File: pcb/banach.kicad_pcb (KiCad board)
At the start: 2 copper layers, 132.3 x 90.7 mm, 68 parts, among them J1 MJ-4PP-9, J2 OLED, SW10 SW_PUSH, SW11 SW_PUSH, SW12 SW_PUSH, SW14 SW_PUSH, SW15 SW_PUSH, SW16 SW_PUSH, SW17 SW_PUSH, SW18 SW_PUSH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

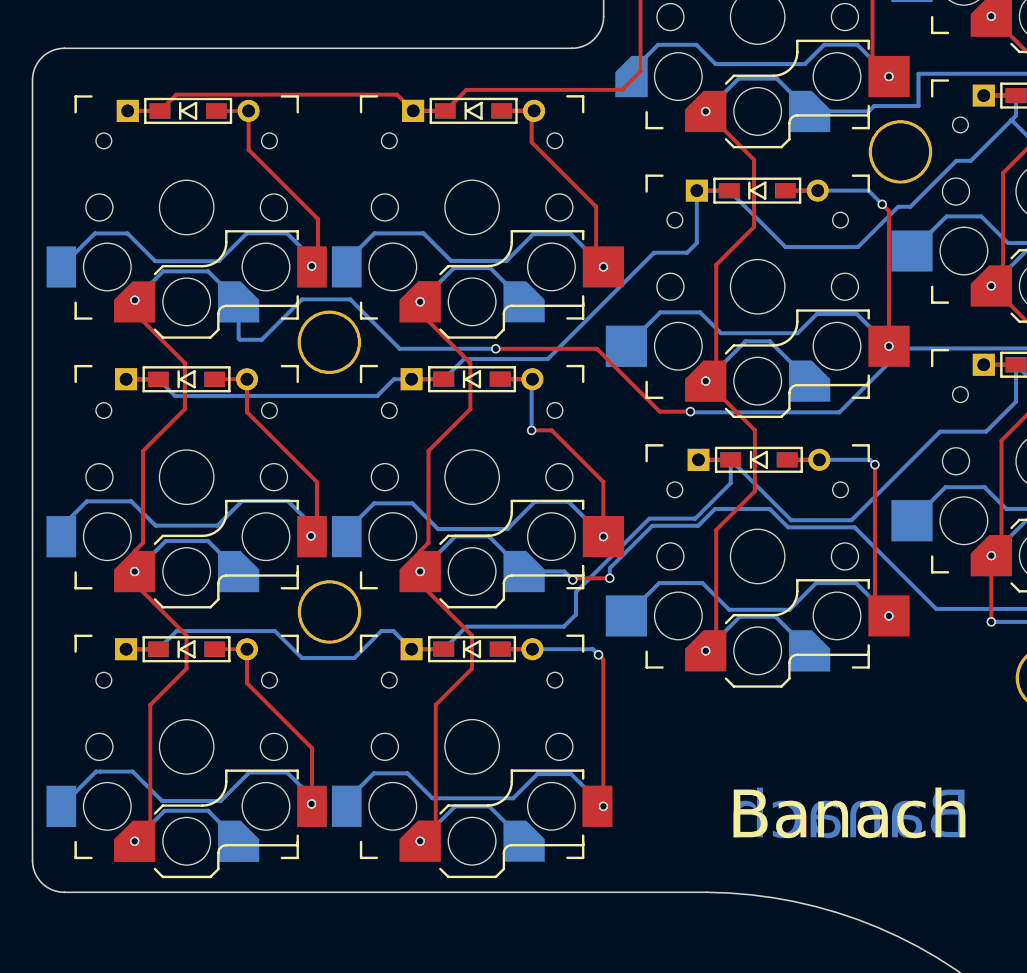
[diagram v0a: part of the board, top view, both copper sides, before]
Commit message: aligned column 0 to true choc spacing
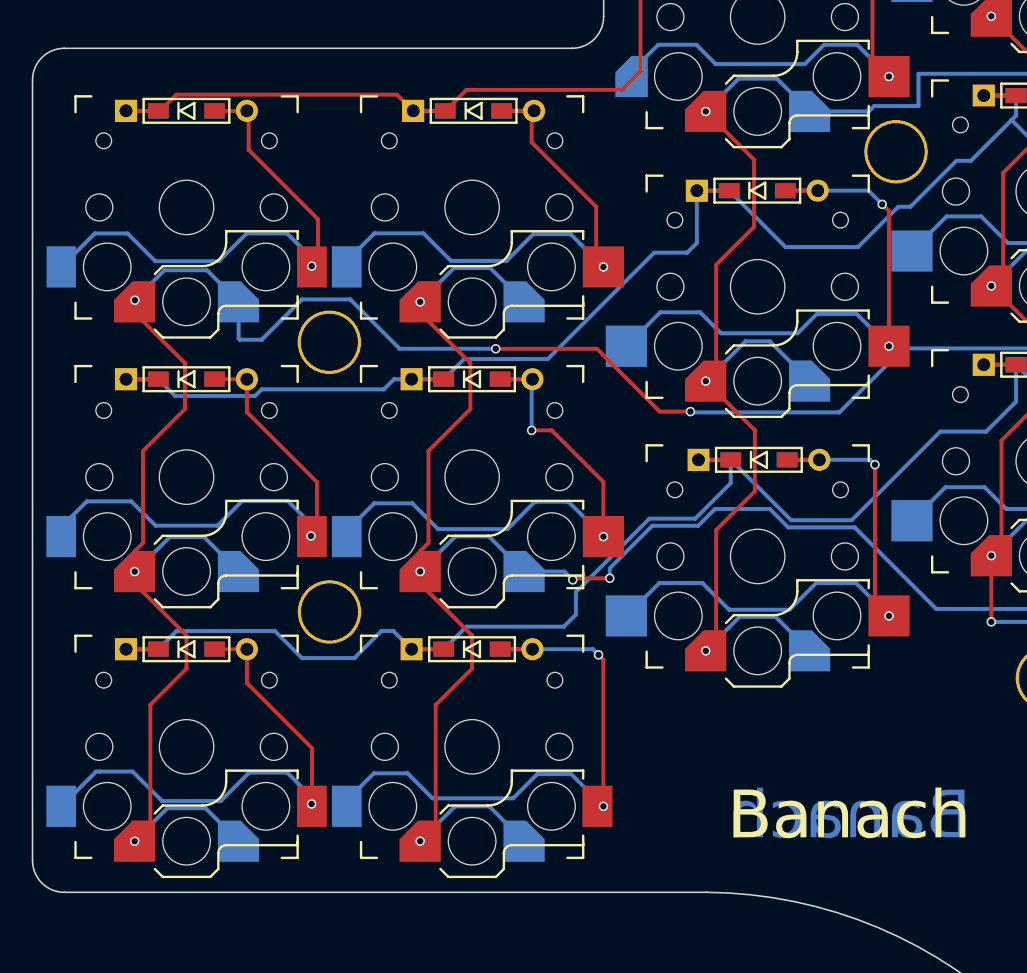
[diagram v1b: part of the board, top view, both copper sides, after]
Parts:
- moved h6 0.28 mm to (112.6, 66.9)
- moved D2 0.11 mm to (67.9, 64.3)
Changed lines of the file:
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@@
   )
   (footprint "kbd:D3_TH_SMD" (layer "F.Cu")
-    (at 67.9088 98.2512)
+    (at 67.9028 98.2472)
     (descr "Resitance 3 pas")
     (tags "R")
@@
   )
   (footprint "kbd:D3_TH_SMD" (layer "F.Cu")
-    (at 68.0104 64.3168)
+    (at 67.9028 64.3128)
     (descr "Resitance 3 pas")
     (tags "R")
@@
   )
   (footprint "keyswitches:Kailh_socket_PG1350_reversible" (layer "F.Cu")
-    (at 67.916 70.404)
+    (at 67.91 70.4)
     (descr "Kailh \"Choc\" PG1350 keyswitch reversible socket mount")
     (tags "kailh,choc")
@@
   )
   (footprint "kbd:LEGO_HOLE" (layer "F.Cu")
-    (at 112.91 66.9)
+    (at 112.63 66.89)
     (descr "Mounting Hole 2.2mm, no annular, M2")
     (tags "mounting hole 2.2mm no annular m2")
@@
   )
   (footprint "kbd:D3_TH_SMD" (layer "F.Cu")
-    (at 67.9088 81.2332)
+    (at 67.9028 81.2292)
     (descr "Resitance 3 pas")
     (tags "R")
@@
   )
   (footprint "keyswitches:Kailh_socket_PG1350_reversible" (layer "F.Cu")
-    (at 67.916 87.404)
+    (at 67.91 87.4)
     (descr "Kailh \"Choc\" PG1350 keyswitch reversible socket mount")
     (tags "kailh,choc")
@@
   )
   (footprint "keyswitches:Kailh_socket_PG1350_reversible" (layer "F.Cu")
-    (at 67.916 104.404)
+    (at 67.91 104.4)
     (descr "Kailh \"Choc\" PG1350 keyswitch reversible socket mount")
     (tags "kailh,choc")
@@
   (segment (start 80.988198 81.2292) (end 82.0928 81.2292) (width 0.25) (layer "B.Cu") (net 2))
   (segment (start 171.27 73.4994) (end 179.45 73.4994) (width 0.25) (layer "B.Cu") (net 2))
+  (segment (start 80.347398 81.87) (end 80.988198 81.2292) (width 0.25) (layer "B.Cu") (net 2))
   (segment (start 102.111 69.342) (end 100.076 69.342) (width 0.25) (layer "B.Cu") (net 2))
   (segment (start 121.7168 66.7004) (end 119.9134 64.897) (width 0.25) (layer "B.Cu") (net 2))
   (segment (start 105.667 72.898) (end 102.111 69.342) (width 0.25) (layer "B.Cu") (net 2))
   (segment (start 165.908303 75.120301) (end 167.529204 73.4994) (width 0.25) (layer "B.Cu") (net 2))
+  (segment (start 67.184299 82.283699) (end 72.226301 82.283699) (width 0.25) (layer "B.Cu") (net 2))
   (segment (start 154.4828 72.4916) (end 152.5524 72.4916) (width 0.25) (layer "B.Cu") (net 2))
+  (segment (start 72.226301 82.283699) (end 72.64 81.87) (width 0.25) (layer "B.Cu") (net 2))
   (segment (start 112.776 70.358) (end 110.236 72.898) (width 0.25) (layer "B.Cu") (net 2))
   (segment (start 133.59632 67.35312) (end 125.16352 67.35312) (width 0.25) (layer "B.Cu") (net 2))
   (segment (start 99.4664 73.2536) (end 97.3836 73.2536) (width 0.25) (layer "B.Cu") (net 2))
-  (segment (start 79.933699 82.283699) (end 80.988198 81.2292) (width 0.25) (layer "B.Cu") (net 2))
   (segment (start 136.144 69.9008) (end 133.59632 67.35312) (width 0.25) (layer "B.Cu") (net 2))
   (segment (start 151.07152 73.97248) (end 142.25068 73.97248) (width 0.25) (layer "B.Cu") (net 2))
@@
   (segment (start 90.6822 79.955) (end 85.402 79.955) (width 0.25) (layer "B.Cu") (net 2))
   (segment (start 110.236 72.898) (end 105.667 72.898) (width 0.25) (layer "B.Cu") (net 2))
-  (segment (start 67.184299 82.283699) (end 79.933699 82.283699) (width 0.25) (layer "B.Cu") (net 2))
+  (segment (start 72.64 81.87) (end 80.347398 81.87) (width 0.25) (layer "B.Cu") (net 2))
   (segment (start 97.3836 73.2536) (end 90.6822 79.955) (width 0.25) (layer "B.Cu") (net 2))
   (segment (start 125.16352 67.35312) (end 124.5108 66.7004) (width 0.25) (layer "B.Cu") (net 2))
@@
   (via (at 64.65 76.25) (size 0.6) (drill 0.4) (layers "F.Cu" "B.Cu") (net 25))
   (segment (start 172.5964 64.6094) (end 179.105002 64.6094) (width 0.25) (layer "B.Cu") (net 25))
-  (segment (start 69.265999 108.428999) (end 66.531001 108.428999) (width 0.25) (layer "B.Cu") (net 25))
+  (segment (start 75.184 76.2) (end 72.644 78.74) (width 0.25) (layer "B.Cu") (net 25))
   (segment (start 99.72 83.32) (end 99.67 83.27) (width 0.25) (layer "B.Cu") (net 25))
+  (segment (start 72.644 78.74) (end 71.262 78.74) (width 0.25) (layer "B.Cu") (net 25))
   (segment (start 152.63 69.92) (end 161.84 69.92) (width 0.25) (layer "B.Cu") (net 25))
+  (segment (start 69.017 91.18) (end 66.85 91.18) (width 0.25) (layer "B.Cu") (net 25))
+  (segment (start 66.69 108.27) (end 64.67 110.29) (width 0.25) (layer "B.Cu") (net 25))
   (segment (start 168.36 66.6794) (end 168.36 64.63) (width 0.25) (layer "B.Cu") (net 25))
-  (segment (start 71.191 93.354) (end 69.265999 91.428999) (width 0.25) (layer "B.Cu") (net 25))
-  (segment (start 64.65 76.22) (end 64.65 76.25) (width 0.25) (layer "B.Cu") (net 25))
   (segment (start 165.0606 66.6994) (end 168.34 66.6994) (width 0.25) (layer "B.Cu") (net 25))
-  (segment (start 71.191 78.669) (end 71.262 78.74) (width 0.25) (layer "B.Cu") (net 25))
-  (segment (start 66.441001 74.428999) (end 64.65 76.22) (width 0.25) (layer "B.Cu") (net 25))
+  (segment (start 71.191 110.354) (end 69.107 108.27) (width 0.25) (layer "B.Cu") (net 25))
+  (segment (start 69.107 108.27) (end 66.69 108.27) (width 0.25) (layer "B.Cu") (net 25))
   (segment (start 78.232 76.2) (end 75.184 76.2) (width 0.25) (layer "B.Cu") (net 25))
+  (segment (start 87.4 79.31) (end 81.342 79.31) (width 0.25) (layer "B.Cu") (net 25))
   (segment (start 168.36 64.63) (end 168.3806 64.6094) (width 0.25) (layer "B.Cu") (net 25))
   (segment (start 181.482 66.986398) (end 181.482 67.1054) (width 0.25) (layer "B.Cu") (net 25))
-  (segment (start 69.265999 74.428999) (end 66.441001 74.428999) (width 0.25) (layer "B.Cu") (net 25))
   (segment (start 142.56 84.6) (end 133.187032 84.6) (width 0.25) (layer "B.Cu") (net 25))
-  (segment (start 75.184 76.2) (end 72.644 78.74) (width 0.25) (layer "B.Cu") (net 25))
   (segment (start 168.3806 64.6094) (end 172.5964 64.6094) (width 0.25) (layer "B.Cu") (net 25))
-  (segment (start 87.4 79.31) (end 81.342 79.31) (width 0.25) (layer "B.Cu") (net 25))
-  (segment (start 66.531001 108.428999) (end 64.67 110.29) (width 0.25) (layer "B.Cu") (net 25))
-  (segment (start 71.262 78.74) (end 72.644 78.74) (width 0.25) (layer "B.Cu") (net 25))
-  (segment (start 71.191 110.354) (end 69.265999 108.428999) (width 0.25) (layer "B.Cu") (net 25))
+  (segment (start 66.51 74.36) (end 64.65 76.22) (width 0.25) (layer "B.Cu") (net 25))
+  (segment (start 64.65 76.22) (end 64.65 76.25) (width 0.25) (layer "B.Cu") (net 25))
   (segment (start 113.0887 79.2913) (end 109.06 83.32) (width 0.25) (layer "B.Cu") (net 25))
   (segment (start 109.06 83.32) (end 99.72 83.32) (width 0.25) (layer "B.Cu") (net 25))
+  (segment (start 168.34 66.6994) (end 168.36 66.6794) (width 0.25) (layer "B.Cu") (net 25))
+  (segment (start 71.262 78.74) (end 71.191 78.669) (width 0.25) (layer "B.Cu") (net 25))
   (segment (start 71.191 78.669) (end 71.191 76.354) (width 0.25) (layer "B.Cu") (net 25))
-  (segment (start 66.601001 91.428999) (end 64.74 93.29) (width 0.25) (layer "B.Cu") (net 25))
-  (segment (start 168.34 66.6994) (end 168.36 66.6794) (width 0.25) (layer "B.Cu") (net 25))
   (segment (start 81.342 79.31) (end 78.232 76.2) (width 0.25) (layer "B.Cu") (net 25))
-  (segment (start 69.265999 91.428999) (end 66.601001 91.428999) (width 0.25) (layer "B.Cu") (net 25))
   (segment (start 133.187032 84.6) (end 129.7278 81.140768) (width 0.25) (layer "B.Cu") (net 25))
   (segment (start 129.7278 81.140768) (end 129.7278 80.5578) (width 0.25) (layer "B.Cu") (net 25))
   (segment (start 161.84 69.92) (end 165.0606 66.6994) (width 0.25) (layer "B.Cu") (net 25))
+  (segment (start 71.191 76.354) (end 69.197 74.36) (width 0.25) (layer "B.Cu") (net 25))
+  (segment (start 71.191 93.354) (end 69.017 91.18) (width 0.25) (layer "B.Cu") (net 25))
   (segment (start 129.7278 80.5578) (end 128.4613 79.2913) (width 0.25) (layer "B.Cu") (net 25))
   (segment (start 128.4613 79.2913) (end 113.0887 79.2913) (width 0.25) (layer "B.Cu") (net 25))
   (segment (start 179.105002 64.6094) (end 181.482 66.986398) (width 0.25) (layer "B.Cu") (net 25))
-  (segment (start 71.191 76.354) (end 69.265999 74.428999) (width 0.25) (layer "B.Cu") (net 25))
+  (segment (start 66.85 91.18) (end 64.74 93.29) (width 0.25) (layer "B.Cu") (net 25))
+  (segment (start 69.197 74.36) (end 66.51 74.36) (width 0.25) (layer "B.Cu") (net 25))
   (segment (start 184.53 69.6454) (end 181.482 69.6454) (width 0.25) (layer "F.Cu") (net 26))
   (segment (start 185.756 68.4194) (end 184.53 69.6454) (width 0.25) (layer "F.Cu") (net 26))
